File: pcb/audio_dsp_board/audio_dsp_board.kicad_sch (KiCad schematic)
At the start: 31 parts, among them J1 AudioJack3, J2 AudioJack3, SW1 SW_Push, U1 STM32F405RGTx, U3 CS4270, Y1 16MHz

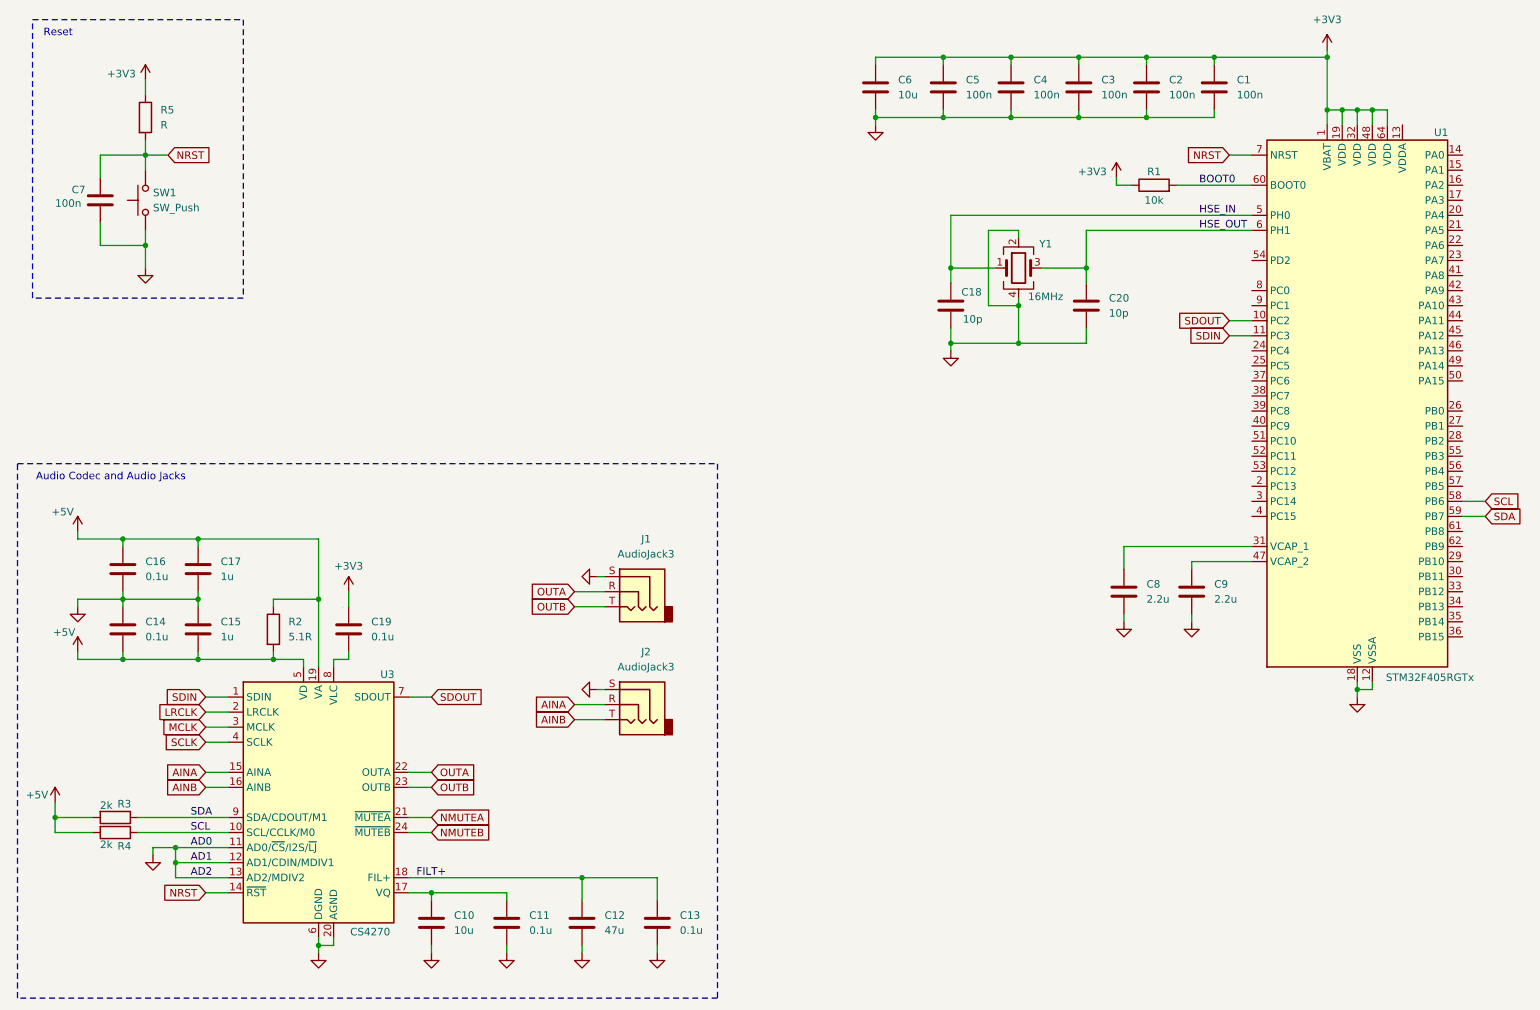
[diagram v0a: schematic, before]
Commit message: Rough draft of schematic capture done
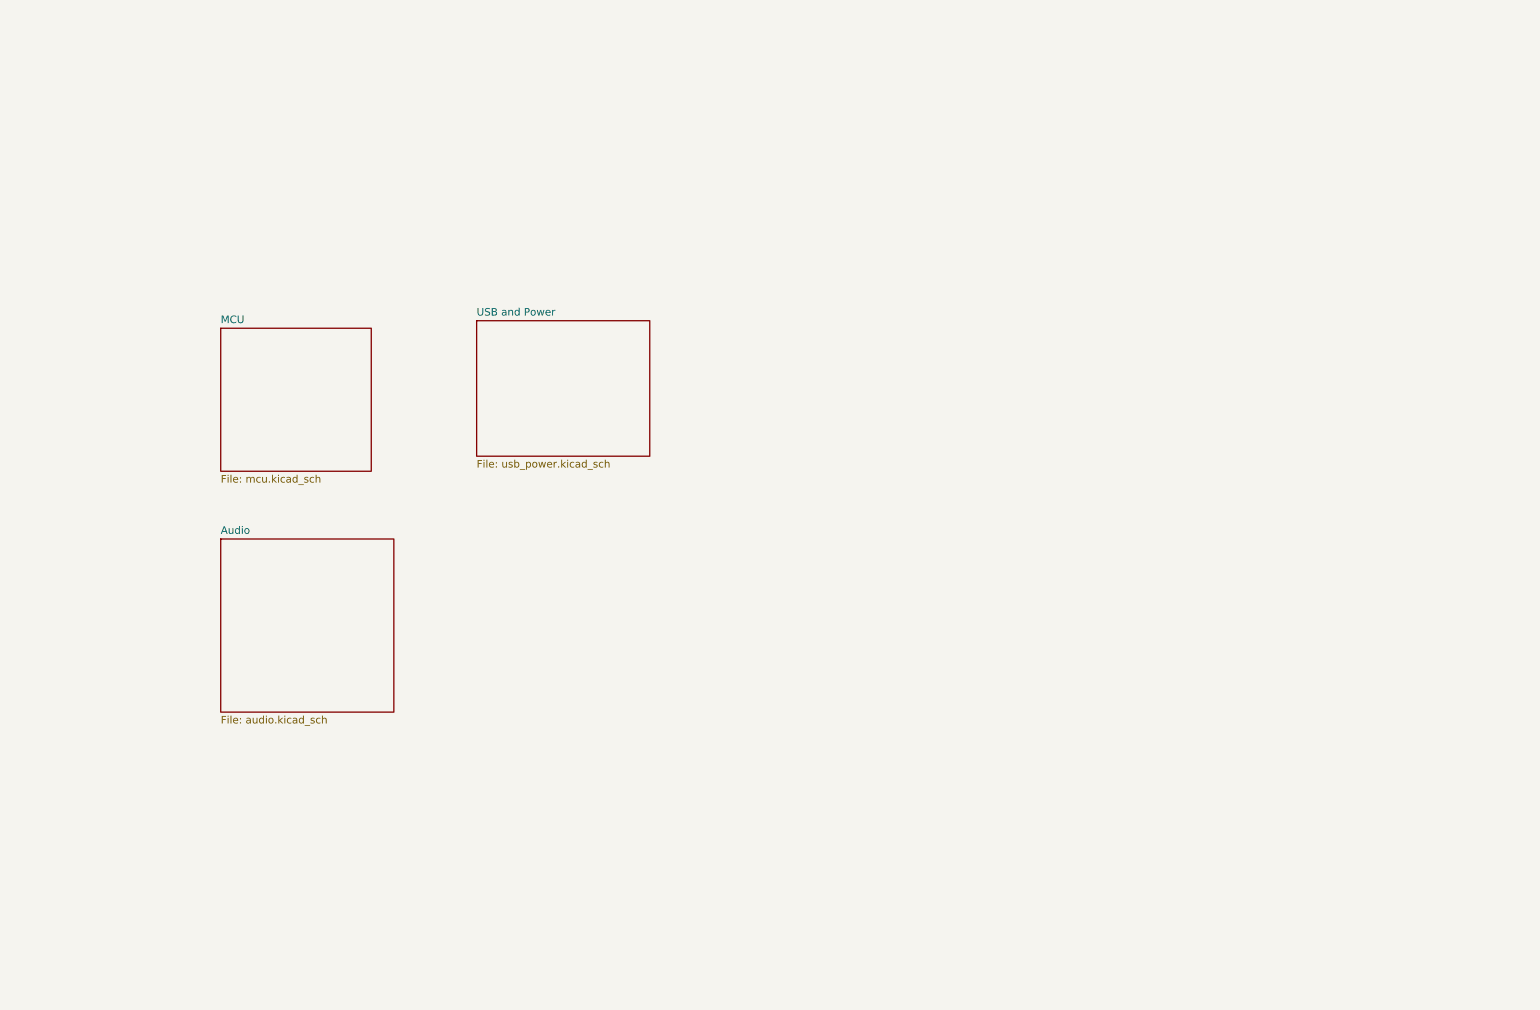
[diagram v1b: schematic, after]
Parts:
- removed C1, C2, C3, C4, C5, C7: 100n, symbol Device:C
- removed C10, C6: 10u, symbol Device:C
- removed C11, C13, C14, C16, C19: 0.1u, symbol Device:C
- removed C12: 47u, symbol Device:C
- removed C15, C17: 1u, symbol Device:C
- removed C18, C20: 10p, symbol Device:C
- removed C8, C9: 2.2u, symbol Device:C
- removed J1, J2: AudioJack3, symbol Connector_Audio:AudioJack3
- removed R1: 10k, symbol Device:R
- removed R2: 5.1R, symbol Device:R
- removed R3, R4: 2k, symbol Device:R
- removed R5: R, symbol Device:R
- removed SW1: SW_Push, symbol Switch:SW_Push
- removed U1: STM32F405RGTx, Package_QFP:LQFP-64_10x10mm_P0.5mm, symbol MCU_ST_STM32F4:STM32F405RGTx
- removed U3: CS4270, Package_SO:TSSOP-24_4.4x7.8mm_P0.65mm, symbol Audio:CS4270
- removed Y1: 16MHz, symbol Device:Crystal_GND24
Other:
- added sheet Audio (audio.kicad_sch)
- added sheet MCU (mcu.kicad_sch)
- added sheet USB and Power (usb_power.kicad_sch)
- note removed: "Audio Codec and Audio Jacks"
- note removed: "Reset"
- title: (none) -> Audio DSP Board

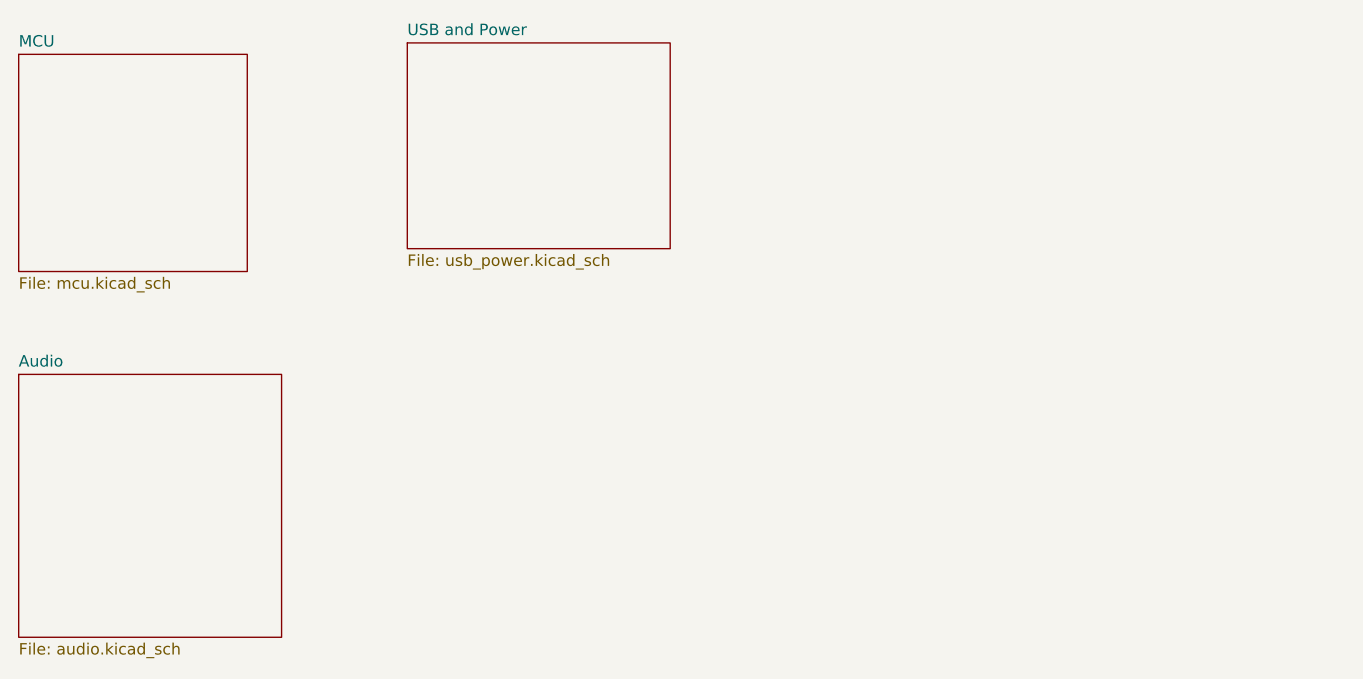
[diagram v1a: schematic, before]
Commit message: Schematic capture, placement, routing complete
Sending board to JLCPCB for manufacturing and assembly.
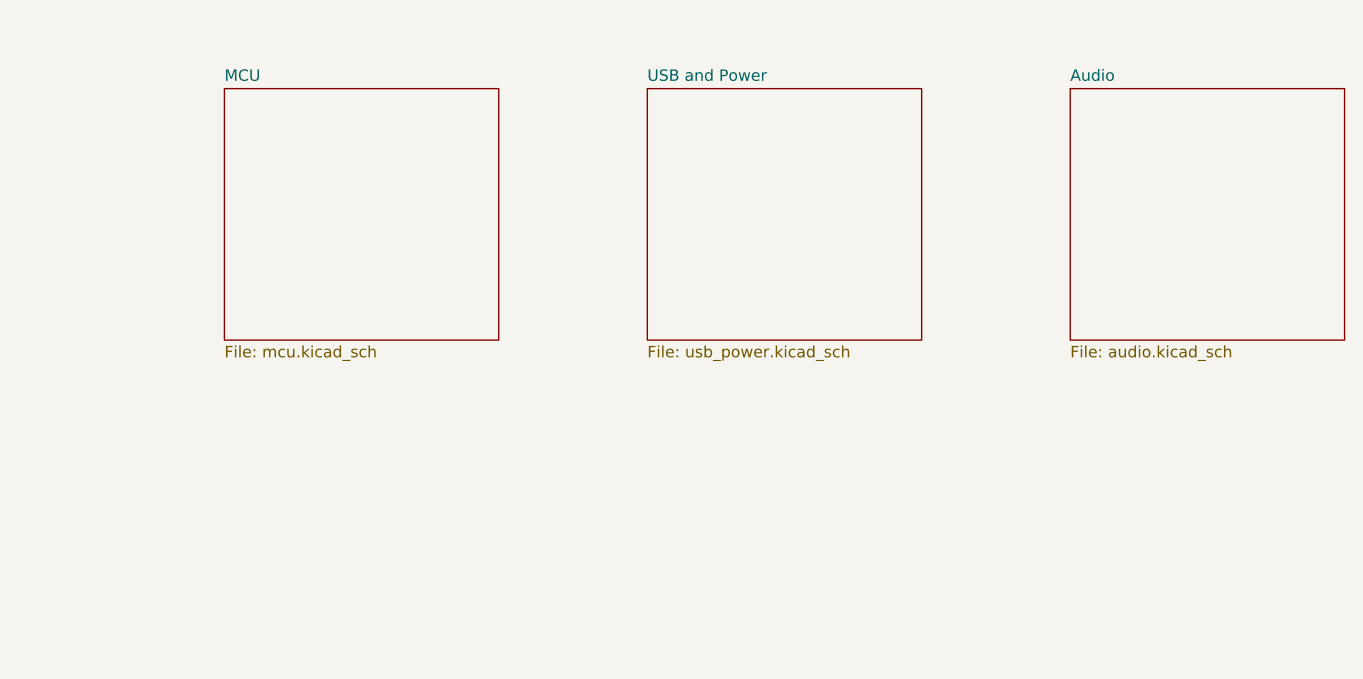
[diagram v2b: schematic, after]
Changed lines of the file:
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@@
 	)
 	(sheet
-		(at 54.61 111.76)
-		(size 29.21 29.21)
+		(at 171.45 80.01)
+		(size 30.48 27.94)
 		(fields_autoplaced yes)
 		(stroke
@@
 		)
 		(property "Sheetname" "Audio"
-			(at 54.61 111.0484 0)
+			(at 171.45 79.2984 0)
 			(effects
 				(font
@@
 		)
 		(property "Sheetfile" "audio.kicad_sch"
-			(at 54.61 141.5546 0)
+			(at 171.45 108.5346 0)
 			(effects
 				(font
@@
 	)
 	(sheet
-		(at 97.79 74.93)
-		(size 29.21 22.86)
+		(at 124.46 80.01)
+		(size 30.48 27.94)
 		(fields_autoplaced yes)
 		(stroke
@@
 		)
 		(property "Sheetname" "USB and Power"
-			(at 97.79 74.2184 0)
+			(at 124.46 79.2984 0)
 			(effects
 				(font
@@
 		)
 		(property "Sheetfile" "usb_power.kicad_sch"
-			(at 97.79 98.3746 0)
+			(at 124.46 108.5346 0)
 			(effects
 				(font
@@
 	)
 	(sheet
-		(at 54.61 76.2)
-		(size 25.4 24.13)
+		(at 77.47 80.01)
+		(size 30.48 27.94)
 		(fields_autoplaced yes)
 		(stroke
@@
 		)
 		(property "Sheetname" "MCU"
-			(at 54.61 75.4884 0)
+			(at 77.47 79.2984 0)
 			(effects
 				(font
@@
 		)
 		(property "Sheetfile" "mcu.kicad_sch"
-			(at 54.61 100.9146 0)
+			(at 77.47 108.5346 0)
 			(effects
 				(font
